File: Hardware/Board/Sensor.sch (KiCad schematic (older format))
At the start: 1 part

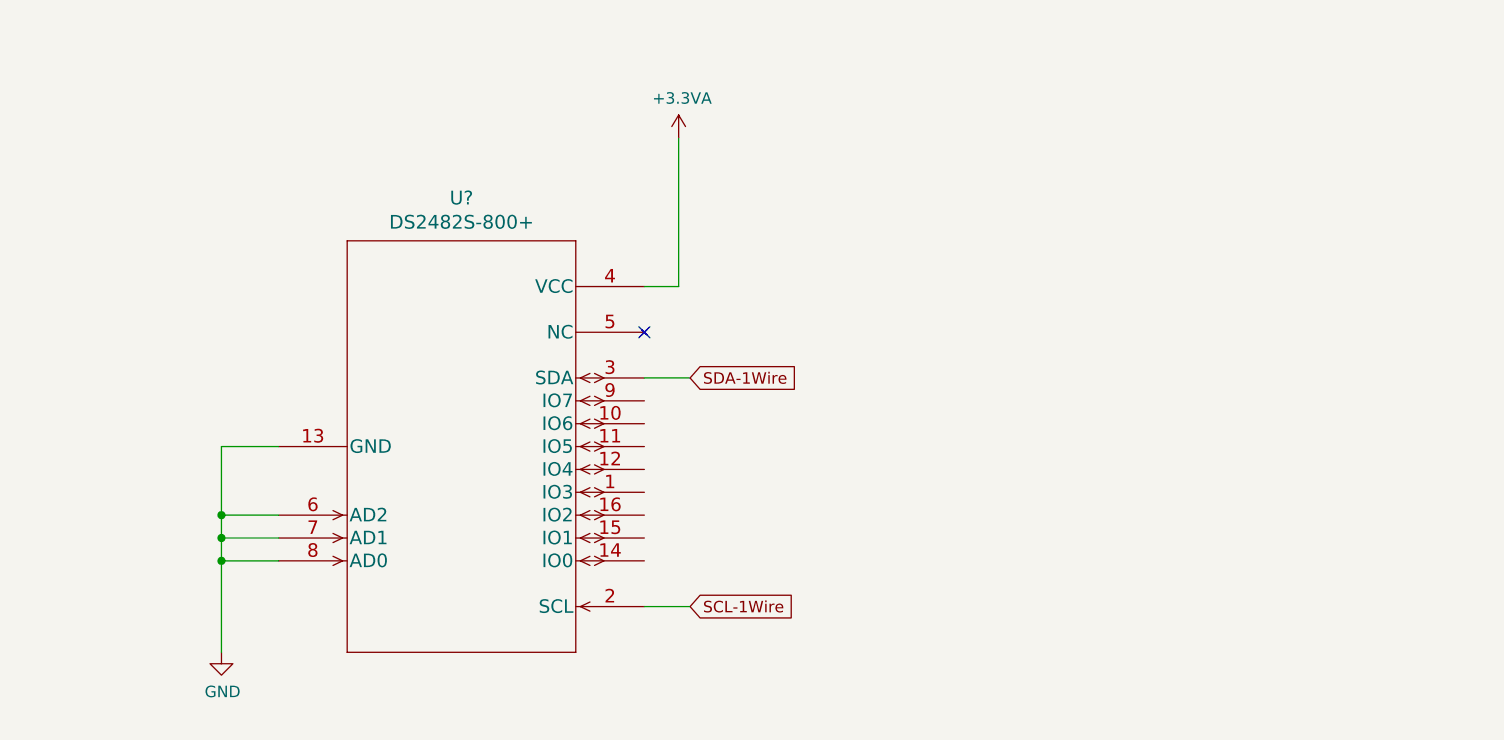
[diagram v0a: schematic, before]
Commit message: JTAG und USB Anschlüsse zugefügt
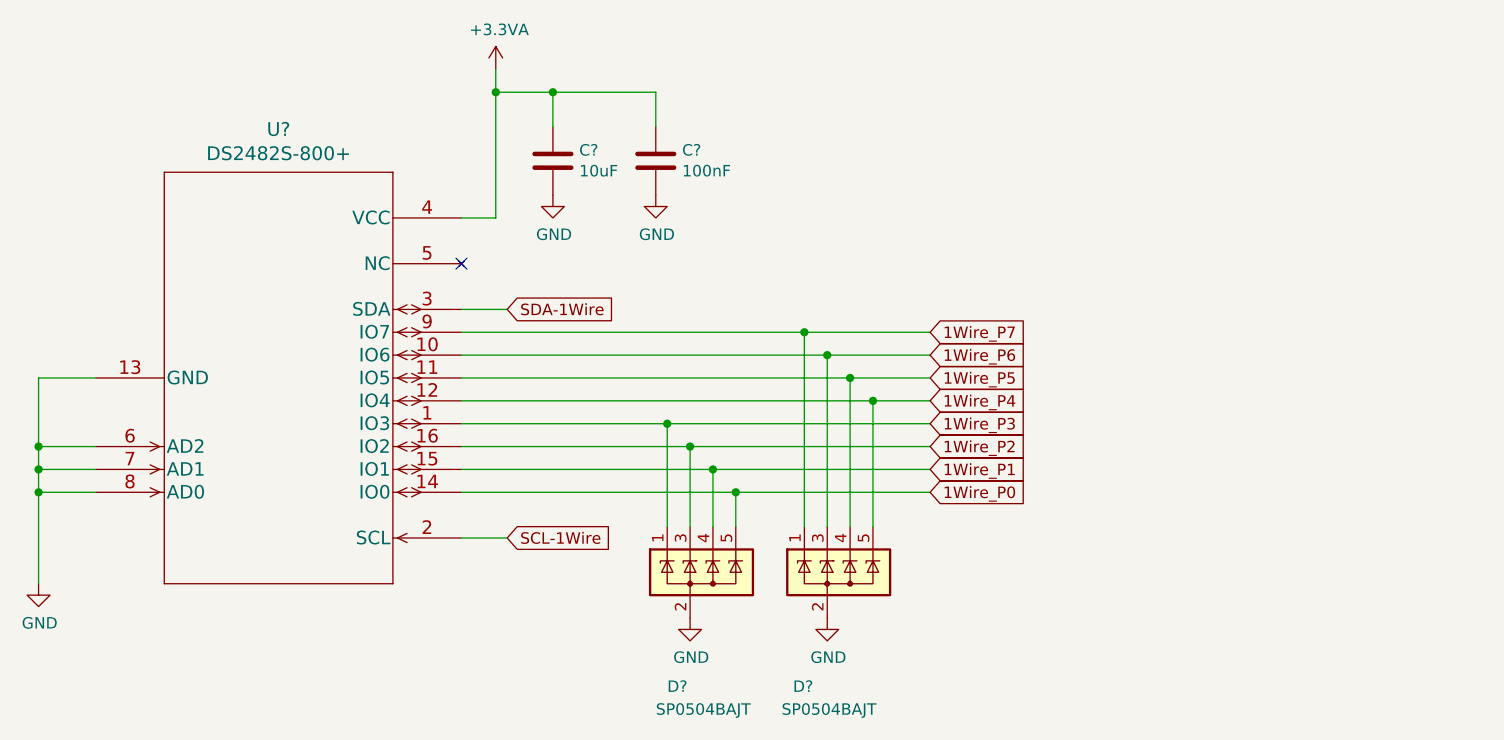
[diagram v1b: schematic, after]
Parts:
- added C?: 10uF, symbol Device:C
- added C?: 100nF, symbol Device:C
- added D? (x2): SP0504BAJT, Package_TO_SOT_SMD:SOT-353_SC-70-5, symbol Power_Protection:SP0504BAJT
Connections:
- net +3.3VA: now also C?.1, C?.1
- net GND: now also C?.2, C?.2, D?.2 (A), D?.2 (A)
- net 1Wire_P3: now reaches U?.1 (IO3)
- net 1Wire_P3: now also D?.1 (K)
- net 1Wire_P6: now reaches U?.10 (IO6)
- net 1Wire_P6: now also D?.3 (K)
- net 1Wire_P5: now reaches U?.11 (IO5)
- net 1Wire_P5: now also D?.4 (K)
- net 1Wire_P4: now reaches U?.12 (IO4)
- net 1Wire_P4: now also D?.5 (K)
- net 1Wire_P0: now reaches U?.14 (IO0)
- net 1Wire_P0: now also D?.5 (K)
- net 1Wire_P1: now reaches U?.15 (IO1)
- net 1Wire_P1: now also D?.4 (K)
- net 1Wire_P2: now reaches U?.16 (IO2)
- net 1Wire_P2: now also D?.3 (K)
- net 1Wire_P7: now reaches U?.9 (IO7)
- net 1Wire_P7: now also D?.1 (K)
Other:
- moved on the sheet: U?

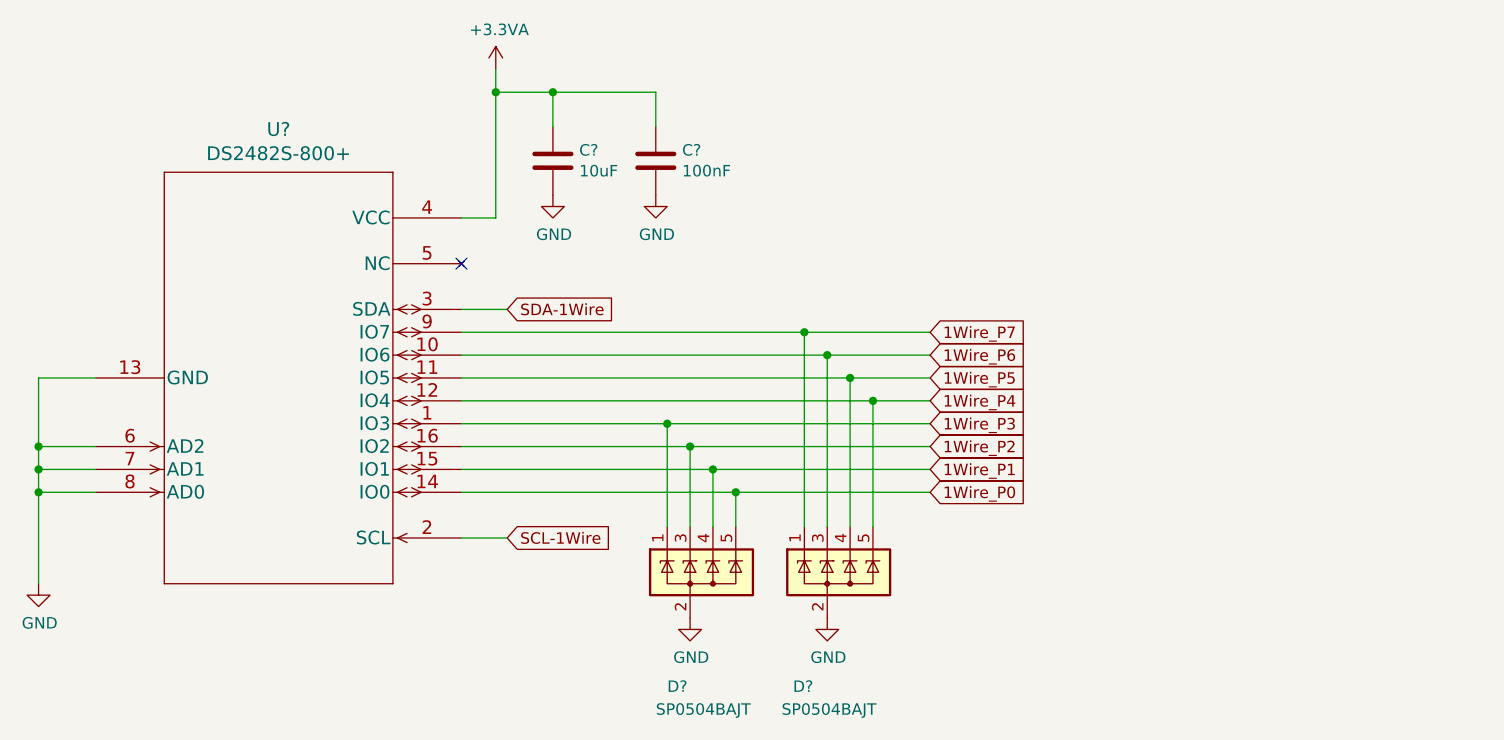
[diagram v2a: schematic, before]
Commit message: 1Wire Power Pull Up. ESP Modul added
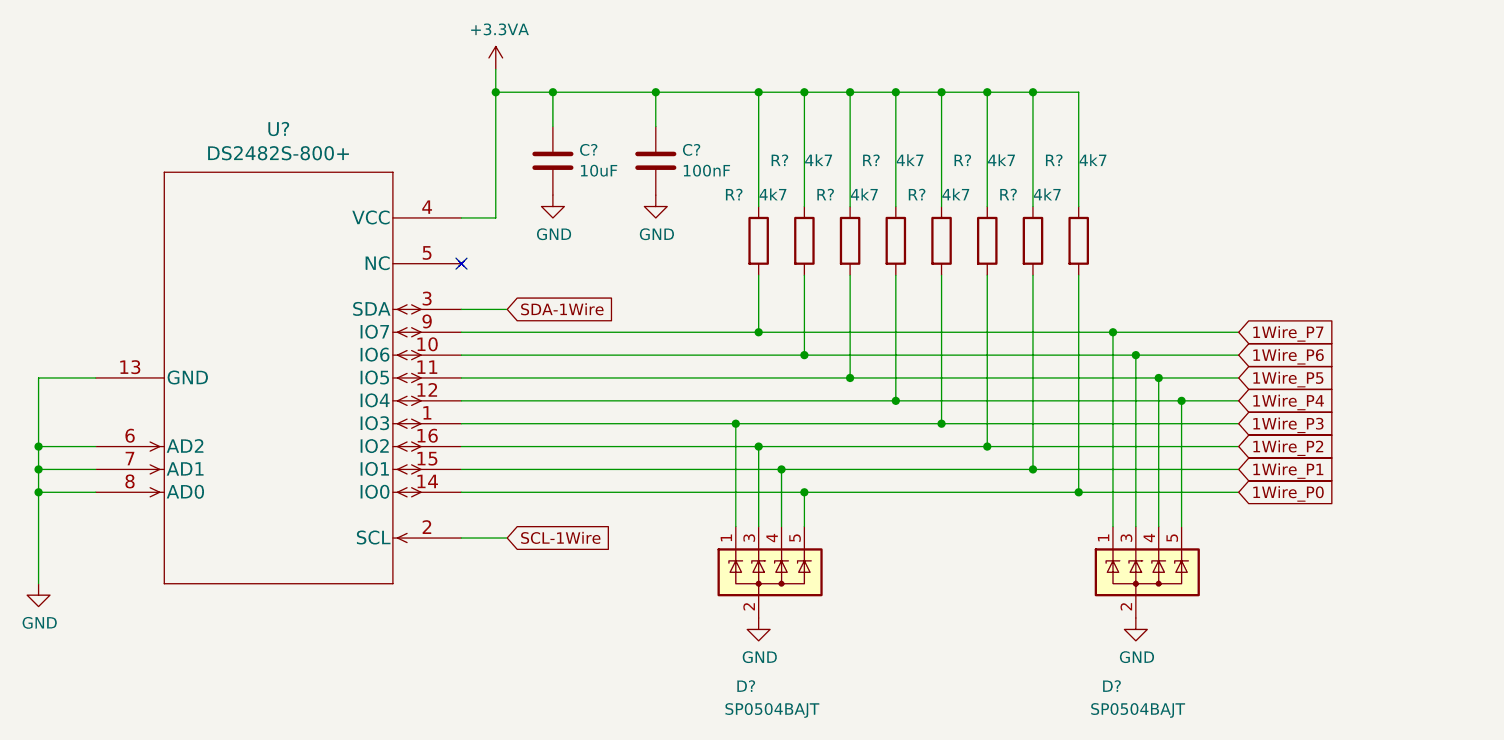
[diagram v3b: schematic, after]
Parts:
- added R? (x8): 4k7, symbol Device:R
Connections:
- net +3.3VA: now also R?.1, R?.1, R?.1, R?.1, R?.1, R?.1, R?.1, R?.1
- net 1Wire_P0: now also R?.2
- net 1Wire_P1: now also R?.2
- net 1Wire_P2: now also R?.2
- net 1Wire_P3: now also R?.2
- net 1Wire_P4: now also R?.2
- net 1Wire_P5: now also R?.2
- net 1Wire_P6: now also R?.2
- net 1Wire_P7: now also R?.2
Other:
- moved on the sheet: D?

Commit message: Netzliste und Board erstellt, hier sind noch Fehler im Bereich Footprints, BLE Modul nRF8001 hinzugefügt, erste Anschlussklemmen zugefügt
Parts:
- added FB10, FB11, FB12, FB13, FB14, FB15, FB8, FB9: 100R, Inductor_SMD:L_0603_1608Metric, symbol Device:Ferrite_Bead_Small
- C61: renamed from C?; footprint (none) -> Capacitor_SMD:C_1210_3225Metric
- C62: renamed from C?; footprint (none) -> Capacitor_SMD:C_0603_1608Metric
- R40, R41, R42, R43, R44, R45, R46, R47: renamed from R?; footprint (none) -> Resistor_SMD:R_0603_1608Metric
- U14: renamed from U?; footprint 21-0041B_16 -> Package_SO:SOIC-16_3.9x9.9mm_P1.27mm
- gave numbers to parts that had none: 2
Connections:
- net 1Wire_P0: now also FB15.1; no longer D12.5 (K), R47.2, U14.14 (IO0)
- net 1Wire_P1: now also FB13.1; no longer D12.4 (K), R46.2, U14.15 (IO1)
- net 1Wire_P2: now also FB11.1; no longer D12.3 (K), R45.2, U14.16 (IO2)
- net 1Wire_P3: now also FB9.1; no longer D12.1 (K), R44.2, U14.1 (IO3)
- net 1Wire_P4: now also FB14.1; no longer D13.5 (K), R43.2, U14.12 (IO4)
- net 1Wire_P5: now also FB12.1; no longer D13.4 (K), R42.2, U14.11 (IO5)
- net 1Wire_P6: now also FB10.1; no longer D13.3 (K), R41.2, U14.10 (IO6)
- net 1Wire_P7: now also FB8.1; no longer D13.1 (K), R40.2, U14.9 (IO7)
- new net: D12.1 (K), FB9.2, R44.2, U14.1 (IO3)
- new net: D13.3 (K), FB10.2, R41.2, U14.10 (IO6)
- new net: D13.4 (K), FB12.2, R42.2, U14.11 (IO5)
- new net: D13.5 (K), FB14.2, R43.2, U14.12 (IO4)
- new net: D12.5 (K), FB15.2, R47.2, U14.14 (IO0)
- new net: D12.4 (K), FB13.2, R46.2, U14.15 (IO1)
- new net: D12.3 (K), FB11.2, R45.2, U14.16 (IO2)
- new net: D13.1 (K), FB8.2, R40.2, U14.9 (IO7)

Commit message: Port Bezeichnungen am Prozessor korrigiert, Schnittstellen angepasst.
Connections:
- net SCL-1Wire renamed I2C1_SCL
- net SDA-1Wire renamed I2C1_SDA
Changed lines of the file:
@@
 $Descr A4 11693 8268
 encoding utf-8
-Sheet 6 7
+Sheet 5 7
 Title ""
 Date ""
@@
 	-1   0    0    1
 $EndComp
-Text GLabel 2750 1900 2    50   Input ~ 0
-SDA-1Wire
+Text GLabel 2750 1900 2    50   BiDi ~ 0
+I2C1_SDA
 Text GLabel 2750 2900 2    50   Input ~ 0
-SCL-1Wire
+I2C1_SCL
 $Comp
 L power:+3.3VA #PWR0235

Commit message: Eine Menge Arbeit auf der GPN, fast fertig im Schaltplan.
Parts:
- U14: symbol 2019-03-28_15-45-29:DS2482S-800+ -> Womo-rescue:DS2482S-800+-2019-03-28_15-45-29
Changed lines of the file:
@@
 EESchema Schematic File Version 4
 LIBS:Womo-cache
-EELAYER 26 0
+EELAYER 29 0
 EELAYER END
 $Descr A4 11693 8268
@@
 $EndDescr
 $Comp
-L 2019-03-28_15-45-29:DS2482S-800+ U14
+L Womo-rescue:DS2482S-800+-2019-03-28_15-45-29 U14
 U 1 1 5C9E4327
 P 1750 2200

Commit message: GSM Modul SIM800L eingefügt, Spannung MCU Board umgenannt
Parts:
- removed C61: 10uF, Capacitor_SMD:C_1210_3225Metric, symbol Device:C
- removed C62: 100nF, Capacitor_SMD:C_0603_1608Metric, symbol Device:C
- removed D12, D13: SP0504BAJT, Package_TO_SOT_SMD:SOT-353_SC-70-5, symbol Power_Protection:SP0504BAJT
- removed FB10, FB11, FB12, FB13, FB14, FB15, FB8, FB9: 100R, Inductor_SMD:L_0603_1608Metric, symbol Device:Ferrite_Bead_Small
- removed R40, R41, R42, R43, R44, R45, R46, R47: 4k7, Resistor_SMD:R_0603_1608Metric, symbol Device:R
- removed U14: DS2482S-800+, Package_SO:SOIC-16_3.9x9.9mm_P1.27mm, symbol Womo-rescue:DS2482S-800+-2019-03-28_15-45-29
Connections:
- no-connect marks 1 -> 0
